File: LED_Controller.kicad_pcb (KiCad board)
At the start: 2 copper layers, 127 x 101.6 mm, 43 parts, among them CON1 CONNECTOR, CON2 CONNECTOR, CON3 CONNECTOR, CON4 CONNECTOR, CON5 PWR_CON, CON6 AVR-ISP-10, CON7 CONNECTOR, IC1 ATMEGA328P-P, Q1 STS8DN3LLH5, Q2 STS8DN3LLH5, Q3 STS8DN3LLH5

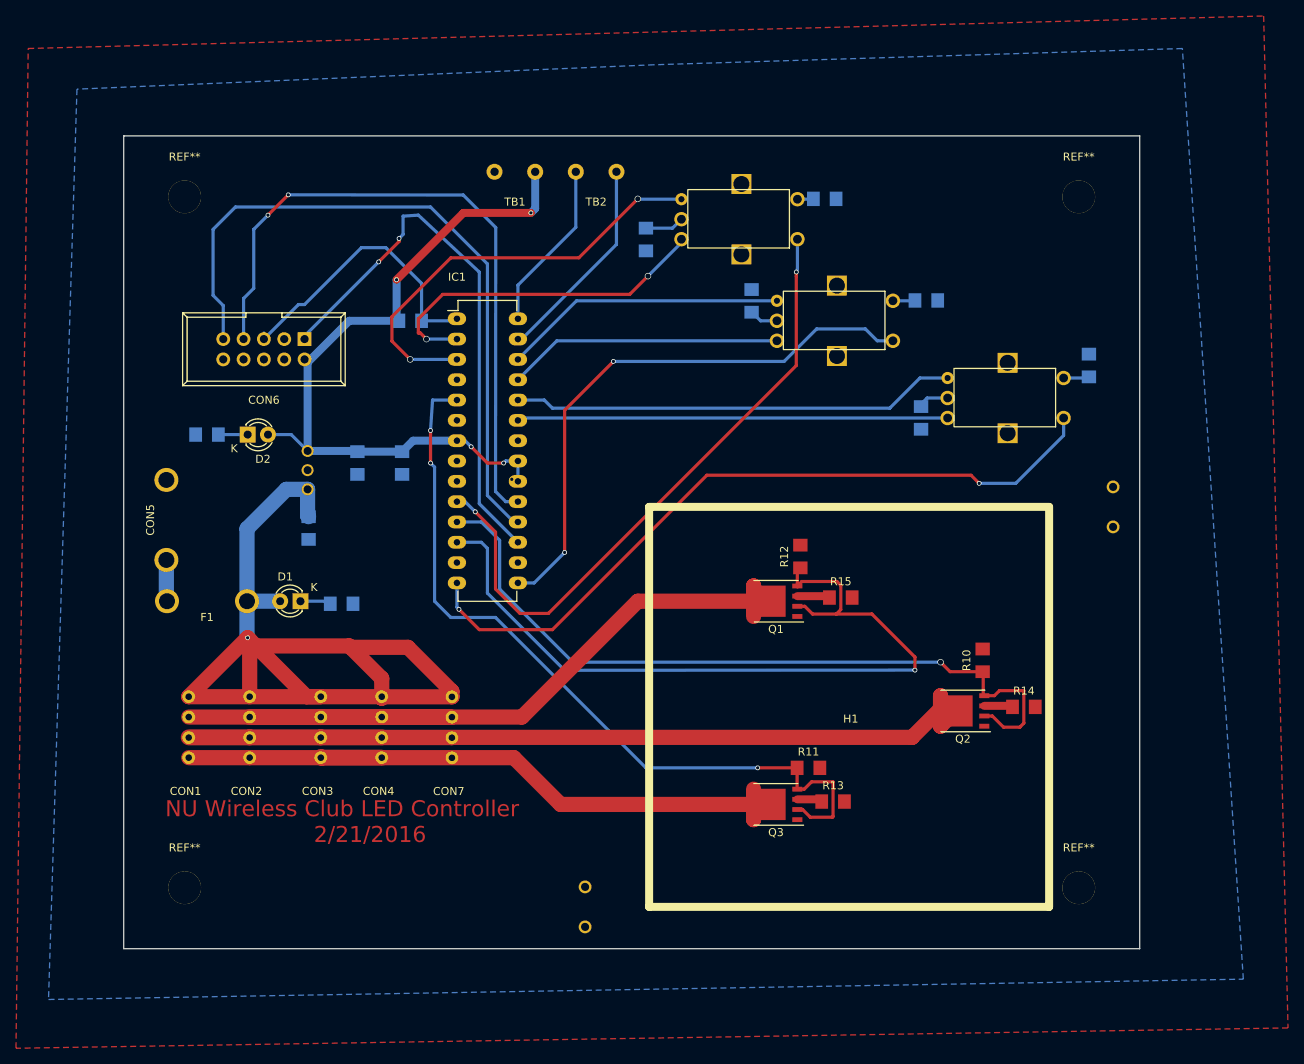
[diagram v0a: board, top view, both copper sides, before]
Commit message: Minor Changes
Removed hidden unconnected via

Re-exported gerbers and drill file
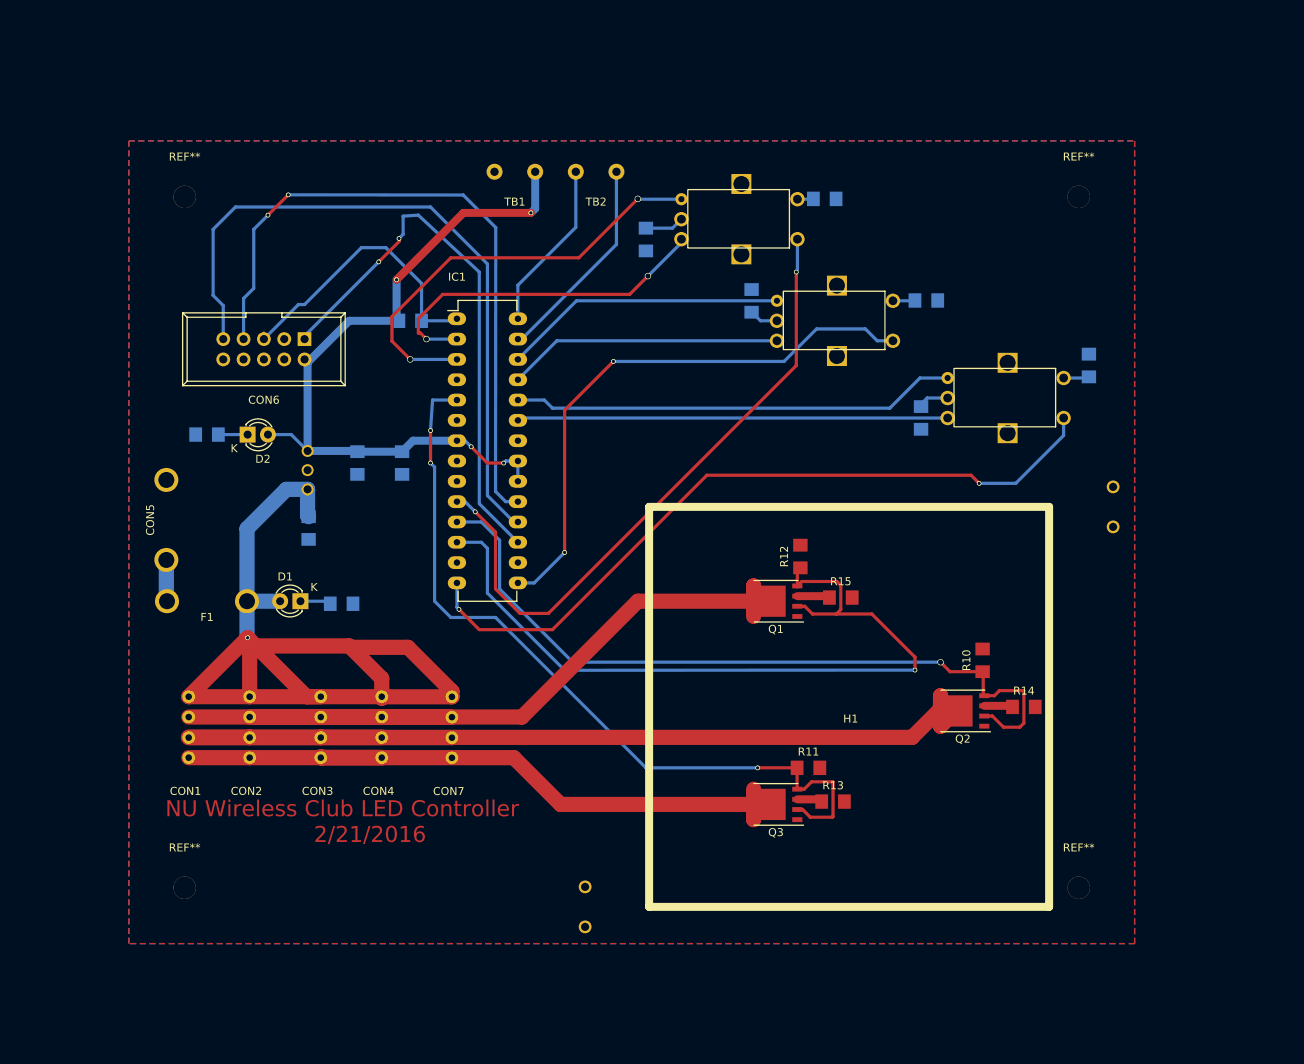
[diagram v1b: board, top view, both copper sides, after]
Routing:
- net +5V: vias 5 -> 4
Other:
- board outline removed
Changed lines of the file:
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@@
     (links 112)
     (no_connects 4)
-    (area 64.008 37.084 223.012001 166.116001)
+    (area 78.029 48.315 203.835001 153.035001)
     (thickness 1.6)
-    (drawings 5)
-    (tracks 307)
+    (drawings 1)
+    (tracks 306)
     (zones 0)
     (modules 43)
@@
     (mod_text_size 1 1)
     (mod_text_width 0.15)
-    (pad_size 3 3)
-    (pad_drill 2)
+    (pad_size 2.8 2.8)
+    (pad_drill 2.8)
     (pad_to_mask_clearance 0.2)
     (aux_axis_origin 74.5 92.5)
@@
       (effects (font (size 1 1) (thickness 0.15)))
     )
-    (pad 1 thru_hole circle (at 0 0) (size 4.1 4.1) (drill 4.1) (layers *.Cu *.Mask F.SilkS))
+    (pad 1 thru_hole circle (at 0 0) (size 2.8 2.8) (drill 2.8) (layers *.Cu *.Mask F.SilkS)
+      (solder_mask_margin 2) (solder_paste_margin 2) (clearance 2) (zone_connect 0) (thermal_width 2) (thermal_gap 2))
   )
   (module LED_controller_footprints:MOUNTING_HOLE (layer F.Cu)
@@
       (effects (font (size 1 1) (thickness 0.15)))
     )
-    (pad 1 thru_hole circle (at 0 0) (size 4.1 4.1) (drill 4.1) (layers *.Cu *.Mask F.SilkS))
+    (pad 1 thru_hole circle (at 0 0) (size 2.8 2.8) (drill 2.8) (layers *.Cu *.Mask F.SilkS)
+      (clearance 2))
   )
   (module LED_controller_footprints:MOUNTING_HOLE (layer F.Cu)
@@
       (effects (font (size 1 1) (thickness 0.15)))
     )
-    (pad 1 thru_hole circle (at 0 0) (size 4.1 4.1) (drill 4.1) (layers *.Cu *.Mask F.SilkS))
+    (pad 1 thru_hole circle (at 0 0) (size 2.8 2.8) (drill 2.8) (layers *.Cu *.Mask F.SilkS)
+      (clearance 2))
   )
   (module LED_controller_footprints:MOUNTING_HOLE (layer F.Cu)
@@
       (effects (font (size 1 1) (thickness 0.15)))
     )
-    (pad 1 thru_hole circle (at 0 0) (size 4.1 4.1) (drill 4.1) (layers *.Cu *.Mask F.SilkS))
+    (pad 1 thru_hole circle (at 0 0) (size 2.8 2.8) (drill 2.8) (layers *.Cu *.Mask F.SilkS)
+      (clearance 2))
   )
   (gr_text "NU Wireless Club LED Controller\n		2/21/2016" (at 104.775 137.795) (layer F.Cu)
     (effects (font (size 2 2) (thickness 0.3)))
   )
-  (gr_line (start 77.47 153.67) (end 77.47 52.07) (angle 90) (layer Edge.Cuts) (width 0.15))
-  (gr_line (start 204.47 153.67) (end 77.47 153.67) (angle 90) (layer Edge.Cuts) (width 0.15))
-  (gr_line (start 204.47 52.07) (end 204.47 153.67) (angle 90) (layer Edge.Cuts) (width 0.15))
-  (gr_line (start 77.47 52.07) (end 204.47 52.07) (angle 90) (layer Edge.Cuts) (width 0.15))
   (segment (start 106.68 91.54414) (end 112.268 91.54414) (width 1) (layer B.Cu) (net 1))
   (segment (start 112.268 91.54414) (end 113.64214 90.17) (width 1) (layer B.Cu) (net 1))
@@
   (segment (start 126.746 92.71) (end 126.746 95.25) (width 0.4) (layer B.Cu) (net 1) (status 30))
   (segment (start 100.076 91.072) (end 100.457 91.453) (width 0.4) (layer B.Cu) (net 1) (status 30))
-  (via (at 125.984 94.996) (size 0.6) (drill 0.4) (layers F.Cu B.Cu) (net 1) (status 30))
   (segment (start 106.56286 91.453) (end 106.68 91.33586) (width 0.4) (layer B.Cu) (net 1) (status 30))
   (segment (start 161.674 109.601) (end 165.50894 109.601) (width 1) (layer F.Cu) (net 2))
@@
   (segment (start 133.985 63.5) (end 133.985 56.555) (width 0.4) (layer B.Cu) (net 33))
   (segment (start 126.746 70.739) (end 133.985 63.5) (width 0.4) (layer B.Cu) (net 33))
+  (zone (net 2) (net_name GND) (layer F.Cu) (hatch edge 0.508)
+    (connect_pads (clearance 0.508))
+    (min_thickness 0.254)
+    (fill yes (arc_segments 16) (thermal_gap 0.508) (thermal_bridge_width 0.508))
+    (polygon
+      (pts
+        (xy 203.835 153.035) (xy 78.105 153.035) (xy 78.105 52.705) (xy 203.835 52.705) (xy 203.835 153.035)
+      )
+    )
+  )
   (zone (net 2) (net_name GND) (layer B.Cu) (hatch edge 0.508)
     (connect_pads (clearance 0.508))
@@
     (polygon
       (pts
-        (xy 143.764 43.18) (xy 71.628 46.228) (xy 68.072 160.02) (xy 217.424 157.48) (xy 209.804 41.148)
-        (xy 143.764 43.18)
+        (xy 203.835 153.035) (xy 78.105 153.035) (xy 78.105 52.705) (xy 203.835 52.705) (xy 203.835 153.035)
       )
     )
-  )
-  (zone (net 2) (net_name GND) (layer F.Cu) (hatch edge 0.508)
-    (connect_pads (clearance 0.508))
-    (min_thickness 0.5)
-    (fill yes (arc_segments 16) (thermal_gap 0.508) (thermal_bridge_width 0.508))
-    (polygon
-      (pts
-        (xy 223.012 163.576) (xy 64.008 166.116) (xy 65.532 41.148) (xy 219.964 37.084) (xy 223.012 163.576)
-      )
-    )
